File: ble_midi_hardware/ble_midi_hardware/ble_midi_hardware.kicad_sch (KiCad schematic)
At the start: 6 parts, among them J1 Conn_01x02_Socket, J2 ESP32_Left, J3 ESP32_Right, J4 Conn_To_Midi_Device, U1 74HC595, U2 74HC595

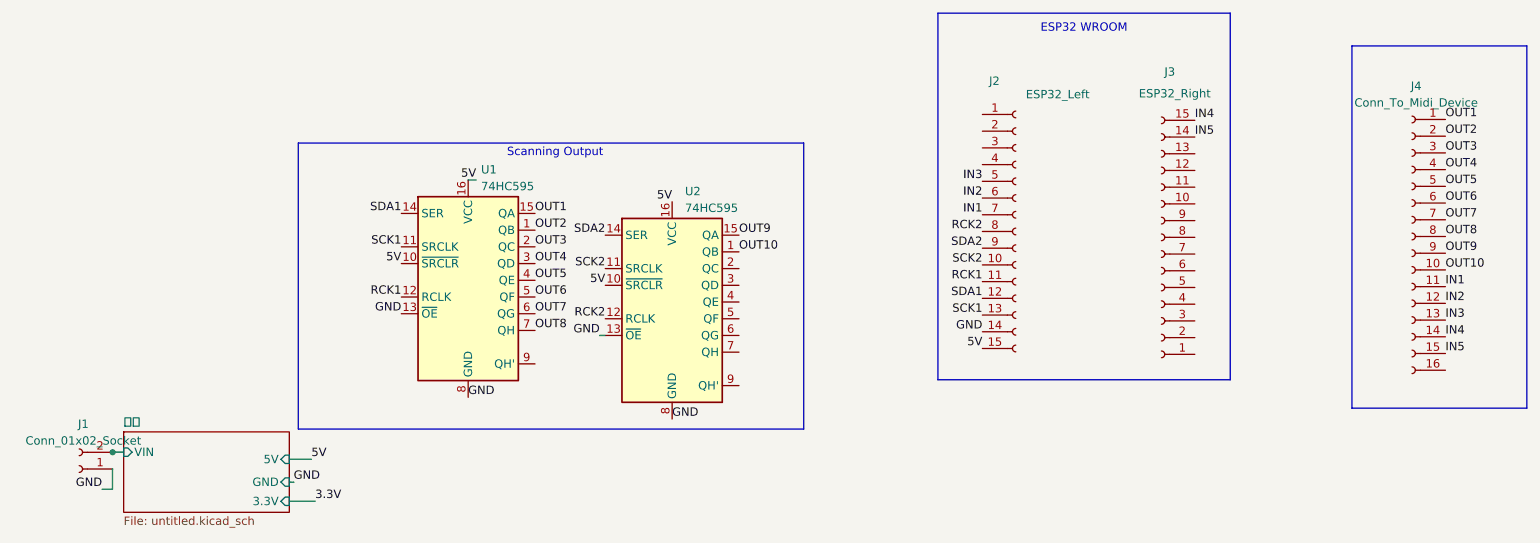
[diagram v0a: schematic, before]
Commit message: 調整HC595供電5V為3.3V以及調整MCU INPUT GPIO pin腳位和部份走線
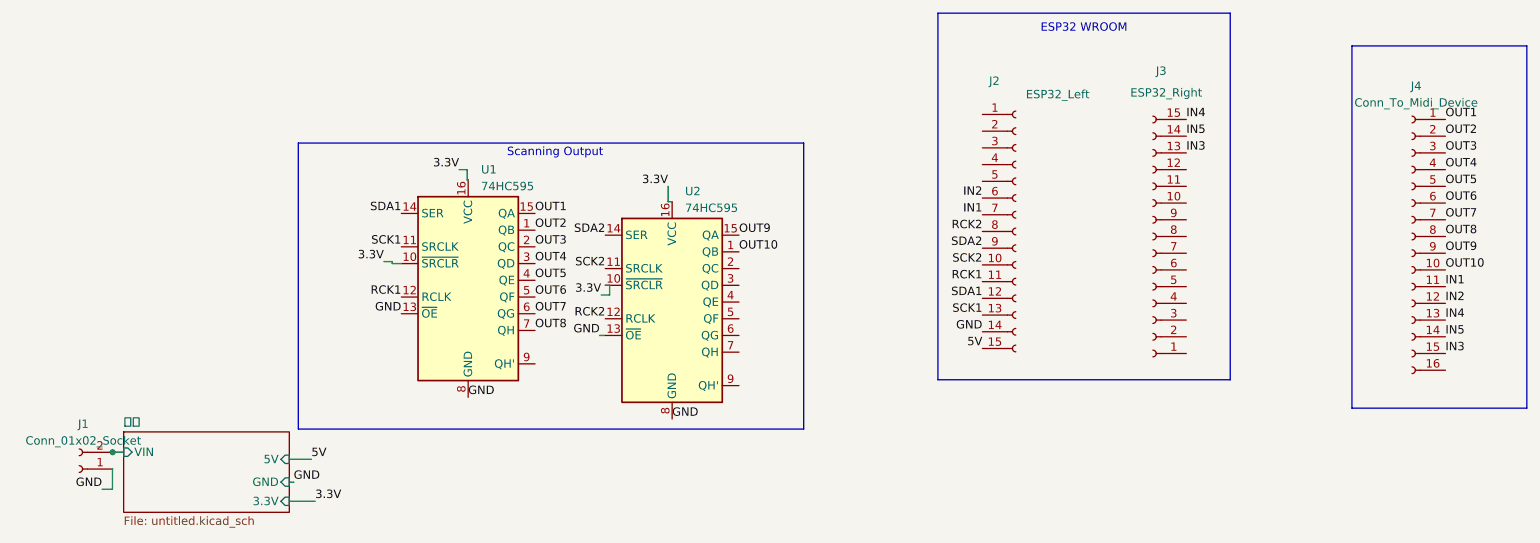
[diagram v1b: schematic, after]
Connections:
- net 3.3V: now also U1.10 (~{SRCLR}), U1.16 (VCC), U2.10 (~{SRCLR}), U2.16 (VCC)
- net 5V: no longer U1.10 (~{SRCLR}), U1.16 (VCC), U2.10 (~{SRCLR}), U2.16 (VCC)
- net IN3: now also J3.13 (Pin_13), J4.15 (Pin_15); no longer J2.5 (Pin_5), J4.13 (Pin_13)
- net IN4: now also J4.13 (Pin_13); no longer J4.14 (Pin_14)
- net IN5: now also J4.14 (Pin_14); no longer J4.15 (Pin_15)

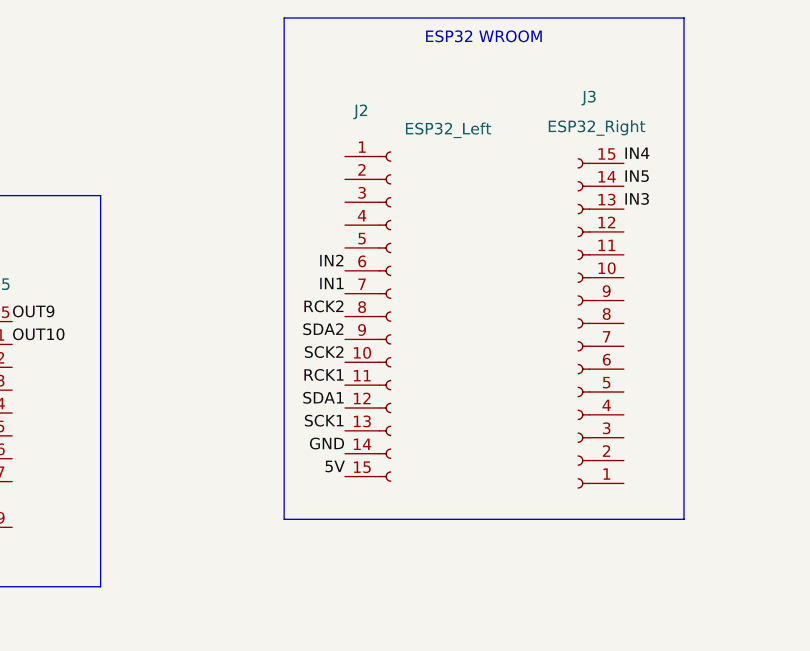
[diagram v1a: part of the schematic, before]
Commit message: 調整SCK2(GPIO25)、RCK2(GPIO26)和SDA2(GPIO27)的腳位位置和pcb走線
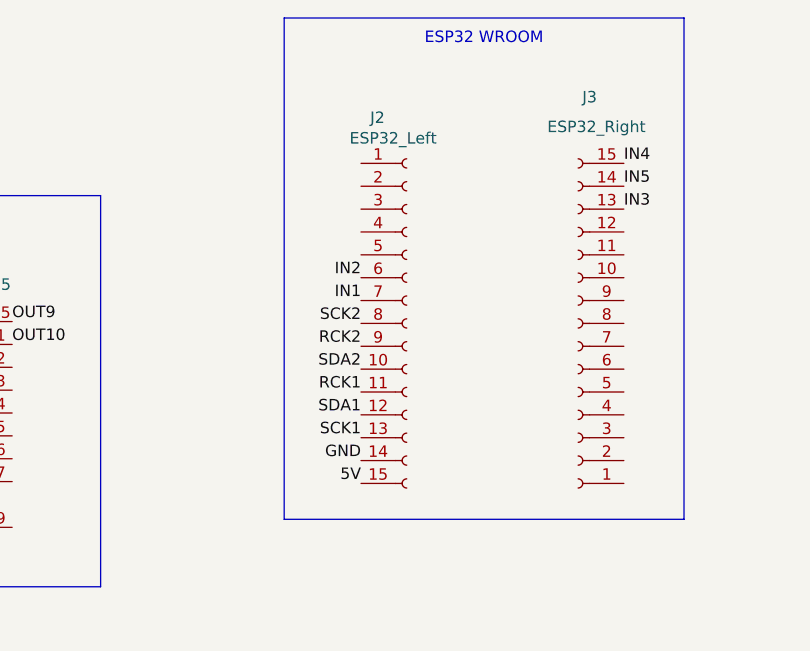
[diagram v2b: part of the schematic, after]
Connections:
- net RCK2: now also J2.9 (Pin_9); no longer J2.8 (Pin_8)
- net SCK2: now also J2.8 (Pin_8); no longer J2.10 (Pin_10)
- net SDA2: now also J2.10 (Pin_10); no longer J2.9 (Pin_9)
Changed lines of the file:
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@@
 	)
 	(label "SCK2"
-		(at 165.862 65.278 180)
+		(at 167.64 60.96 180)
 		(fields_autoplaced yes)
 		(effects
@@
 	)
 	(label "GND"
-		(at 165.862 75.438 180)
+		(at 167.64 76.2 180)
 		(fields_autoplaced yes)
 		(effects
@@
 	)
 	(label "SCK1"
-		(at 165.862 72.898 180)
+		(at 167.64 73.66 180)
 		(fields_autoplaced yes)
 		(effects
@@
 	)
 	(label "SDA2"
-		(at 165.862 62.738 180)
+		(at 167.64 66.04 180)
 		(fields_autoplaced yes)
 		(effects
@@
 	)
 	(label "5V"
-		(at 165.862 77.978 180)
+		(at 167.64 78.74 180)
 		(fields_autoplaced yes)
 		(effects
@@
 	)
 	(label "IN1"
-		(at 165.862 57.658 180)
+		(at 167.64 58.42 180)
 		(fields_autoplaced yes)
 		(effects
@@
 	)
 	(label "IN2"
-		(at 165.862 55.118 180)
+		(at 167.64 55.88 180)
 		(fields_autoplaced yes)
 		(effects
@@
 	)
 	(label "RCK1"
-		(at 165.862 67.818 180)
+		(at 167.64 68.58 180)
 		(fields_autoplaced yes)
 		(effects
@@
 	)
 	(label "SDA1"
-		(at 165.862 70.358 180)
+		(at 167.64 71.12 180)
 		(fields_autoplaced yes)
 		(effects
@@
 	)
 	(label "RCK2"
-		(at 165.862 60.198 180)
+		(at 167.64 63.5 180)
 		(fields_autoplaced yes)
 		(effects
@@
 			)
 			(justify left bottom)
-		)
-	)
-	(symbol
-		(lib_id "Connector:Conn_01x15_Socket")
-		(at 170.942 60.198 0)
-		(unit 1)
-		(exclude_from_sim no)
-		(in_bom yes)
-		(on_board yes)
-		(dnp no)
-		(property "Reference" "J2"
-			(at 166.878 37.338 0)
-			(effects
-				(font
-					(size 1.27 1.27)
-				)
-				(justify left)
-			)
-		)
-		(property "Value" "ESP32_Left"
-			(at 172.466 39.37 0)
-			(effects
-				(font
-					(size 1.27 1.27)
-				)
-				(justify left)
-			)
-		)
-		(property "Footprint" "Connector_PinHeader_2.54mm:PinHeader_1x15_P2.54mm_Vertical"
-			(at 170.942 60.198 0)
-			(effects
-				(font
-					(size 1.27 1.27)
-				)
-				(hide yes)
-			)
-		)
-		(property "Datasheet" "~"
-			(at 170.942 60.198 0)
-			(effects
-				(font
-					(size 1.27 1.27)
-				)
-				(hide yes)
-			)
-		)
-		(property "Description" ""
-			(at 170.942 60.198 0)
-			(effects
-				(font
-					(size 1.27 1.27)
-				)
-				(hide yes)
-			)
-		)
-		(pin "1"
-		)
-		(pin "10"
-		)
-		(pin "11"
-		)
-		(pin "12"
-		)
-		(pin "13"
-		)
-		(pin "14"
-		)
-		(pin "15"
-		)
-		(pin "2"
-		)
-		(pin "3"
-		)
-		(pin "4"
-		)
-		(pin "5"
-		)
-		(pin "6"
-		)
-		(pin "7"
-		)
-		(pin "8"
-		)
-		(pin "9"
-		)
-		(instances
-			(project "ble_midi_hardware"
-				(path "/2430d23c-7a32-4c0f-92aa-bc816bceade1"
-					(reference "J2")
-					(unit 1)
-				)
-			)
 		)
 	)
@@
 					(unit 1)
 				)
+			)
+		)
+	)
+	(symbol
+		(lib_id "Connector:Conn_01x15_Socket")
+		(at 172.72 60.96 0)
+		(unit 1)
+		(exclude_from_sim no)
+		(in_bom yes)
+		(on_board yes)
+		(dnp no)
+		(property "Reference" "J2"
+			(at 168.656 38.1 0)
+			(effects
+				(font
+					(size 1.27 1.27)
+				)
+				(justify left)
+			)
+		)
+		(property "Value" "ESP32_Left"
+			(at 166.37 40.386 0)
+			(effects
+				(font
+					(size 1.27 1.27)
+				)
+				(justify left)
+			)
+		)
+		(property "Footprint" "Connector_PinHeader_2.54mm:PinHeader_1x15_P2.54mm_Vertical"
+			(at 172.72 60.96 0)
+			(effects
+				(font
+					(size 1.27 1.27)
+				)
+				(hide yes)
+			)
+		)
+		(property "Datasheet" "~"
+			(at 172.72 60.96 0)
+			(effects
+				(font
+					(size 1.27 1.27)
+				)
+				(hide yes)
+			)
+		)
+		(property "Description" ""
+			(at 172.72 60.96 0)
+			(effects
+				(font
+					(size 1.27 1.27)
+				)
+				(hide yes)
+			)
+		)
+		(pin "1"
+		)
+		(pin "10"
+		)
+		(pin "11"
+		)
+		(pin "12"
+		)
+		(pin "13"
+		)
+		(pin "14"
+		)
+		(pin "15"
+		)
+		(pin "2"
+		)
+		(pin "3"
+		)
+		(pin "4"
+		)
+		(pin "5"
+		)
+		(pin "6"
+		)
+		(pin "7"
+		)
+		(pin "8"
+		)
+		(pin "9"
+		)
+		(instances
+			(project "ble_midi_hardware"
+				(path "/2430d23c-7a32-4c0f-92aa-bc816bceade1"
+					(reference "J2")
+					(unit 1)
+				)
